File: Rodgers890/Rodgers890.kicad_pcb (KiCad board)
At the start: 2 copper layers, 96.3 x 93.5 mm, 74 parts, among them J1 Conn_01x30_Pin, J2 Conn_01x02_Pin, Q1 BC817, Q2 BC807, Q3 BC817, Q4 BC807, U1 7417, U2 4050

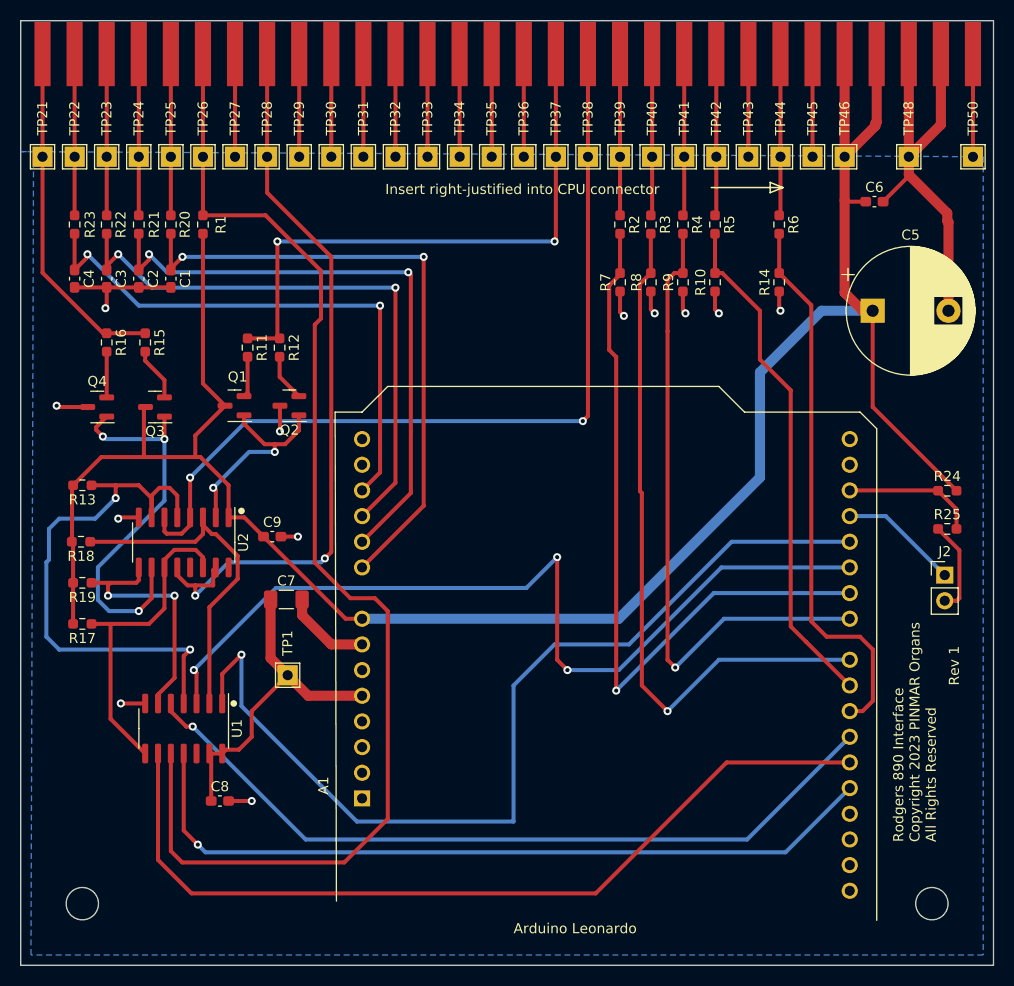
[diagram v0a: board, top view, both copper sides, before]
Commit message: Address Issue #4: Wrong output chain used, for PCB. Revision marking on PCB is "Rev 2".
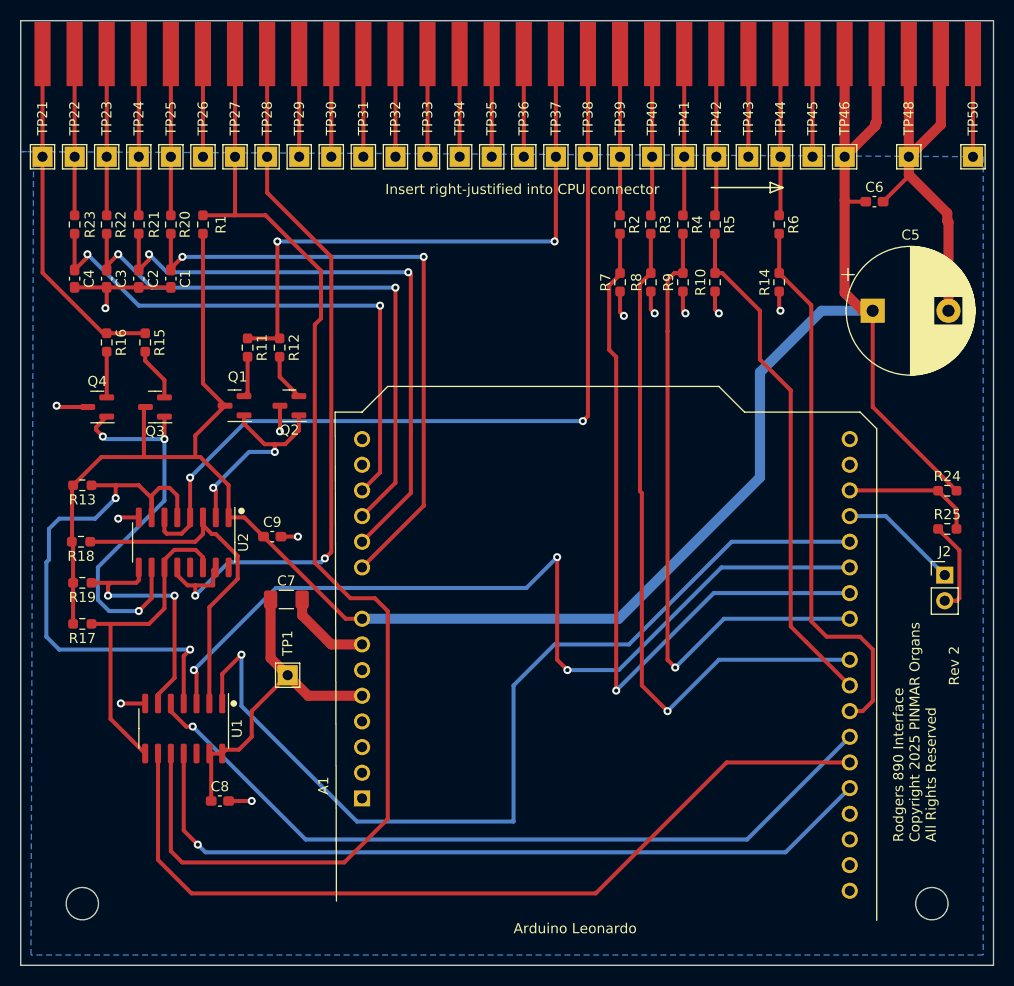
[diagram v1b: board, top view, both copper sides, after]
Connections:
- net /S0_cpu renamed /S6_cpu
- R1 pad 1: /S0 -> /S6
- U1 pad 10: /S0 -> /S6
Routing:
- net /S6: track 10.2 -> 122.2 mm
- net /S0: track 122.2 -> 10.2 mm
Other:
- board text added: "Rev 2"
- board text added: "Rodgers 890 Interface Copyright 2025 PINMAR Organs All Rights Reserved"
- board text removed: "Rev 1"
- board text removed: "Rodgers 890 Interface Copyright 2023 PINMAR Organs All Rights Reserved"
